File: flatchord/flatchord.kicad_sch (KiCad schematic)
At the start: 9 parts, among them J1 OLED SSD1306, SW0 SW_SPST, SW1 SW_SPST, SW2 SW_SPST, SW3 SW_SPST, SW4 SW_SPST, SW5 SW_DPDT_x2, U2 Nice! Nano (ProMicro)

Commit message: named board
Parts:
- removed BT1: Bat JST-GH 1.25, Connector_JST:JST_GH_SM02B-GHS-TB_1x02-1MP_P1.25mm_Horizontal, symbol Device:Battery_Cell
- added BAT1: JST-GH 1.25, footprints:JST_GH_SM02B-GHS-TB_1x02-1MP_P1.25mm_Horizontal, symbol Connector:Conn_01x04_Socket
- J1: footprint Connector_PinHeader_1.00mm:PinHeader_1x04_P1.00mm_Vertical_SMD_Pin1Right -> ssd1306-smd-header:lightblue-ssd1306-smd
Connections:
- net B+: now also SW5.1 (A), BAT1.1 (Pin_1); no longer SW5.2 (B)
- net GND: now also BAT1.2 (Pin_2)
- net RAW: now also SW5.2 (B); no longer SW5.1 (A)
- net middle: now reaches SW1.1 (A), U2.10 (GP7)
- net index: now reaches SW0.1 (A), U2.11 (GP8)
- net thumb: now reaches SW4.1 (A), U2.12 (GP9)
- net pinky: now reaches SW3.1 (A), U2.8 (GP5)
- net ring: now reaches SW2.1 (A), U2.9 (GP6)
- new net mp: BAT1.3 (Pin_3), BAT1.4 (Pin_4)
- no-connect marks 1 -> 3
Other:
- note added: "Fingers"
- note added: "I2C"
- note added: "Power"
- moved on the sheet: SW0, SW2, SW3, SW4, SW5A

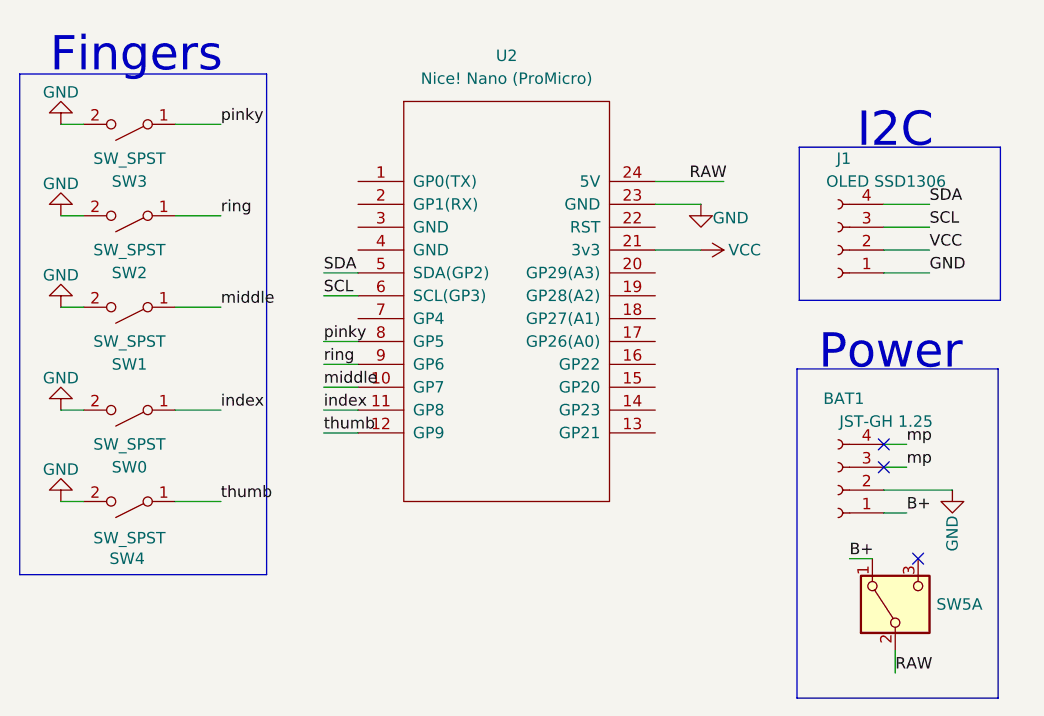
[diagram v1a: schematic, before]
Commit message: significant changes
new display 1.3" SH1106 and ESP32-S3 supermini, big shrink in size
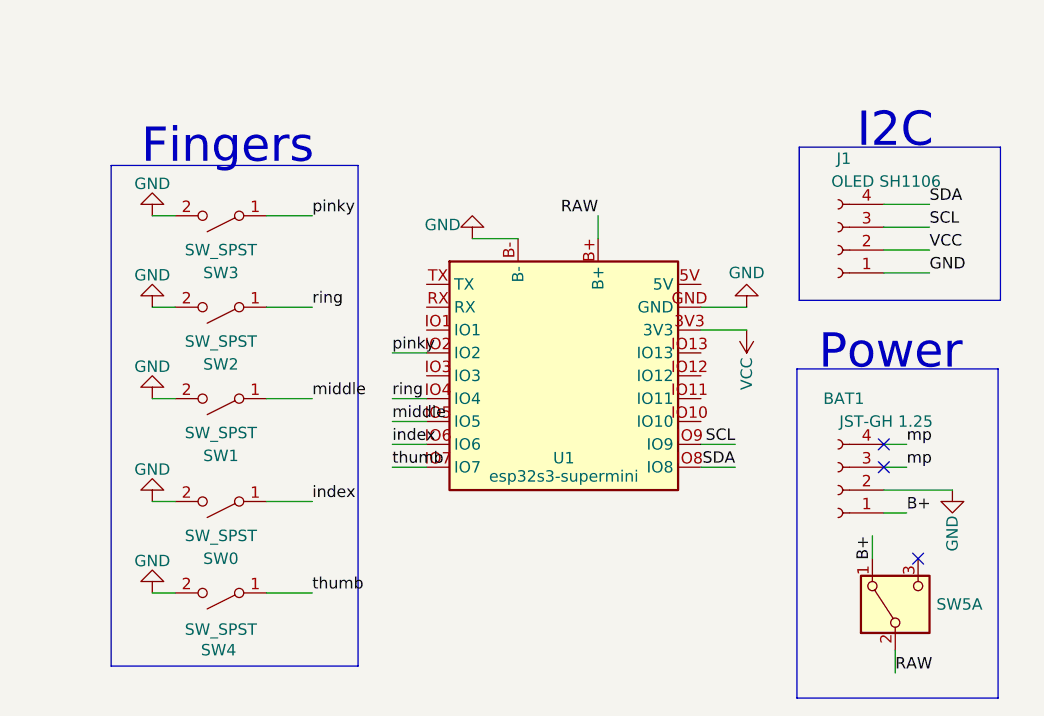
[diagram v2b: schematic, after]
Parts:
- removed U2: Nice! Nano (ProMicro), footprints:nnv2-smd-2x, symbol TheOneProMicro:ProMicro_2-Lily58-cache
- added U1: esp32s3-supermini, ESP32-S3-SuperMini_SMT, symbol esp32s3-supermini:esp32s3-supermini
- J1: value OLED SSD1306 -> OLED SH1106; footprint ssd1306-smd-header:lightblue-ssd1306-smd -> footprints:tft-sh1106-1.3-i2c
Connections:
- net GND: now also U1.B-, U1.GND
- net RAW: now also U1.B+
- net SCL: now also U1.IO9
- net SDA: now also U1.IO8
- net VCC: now also U1.3V3
- net index: now also U1.IO6
- net middle: now also U1.IO5
- net pinky: now also U1.IO2
- net ring: now also U1.IO4
- net thumb: now also U1.IO7
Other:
- moved on the sheet: SW0, SW1, SW2, SW3, SW4
